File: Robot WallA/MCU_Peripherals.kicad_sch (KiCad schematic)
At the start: 44 parts, among them IC3 USBLC6-4SC6, IC4 USBLC6-4SC6, IC5 LAN8742A-CZ-TR, J2 USB4216-03-A, J3 SS-90000-009, T1 H1102NL

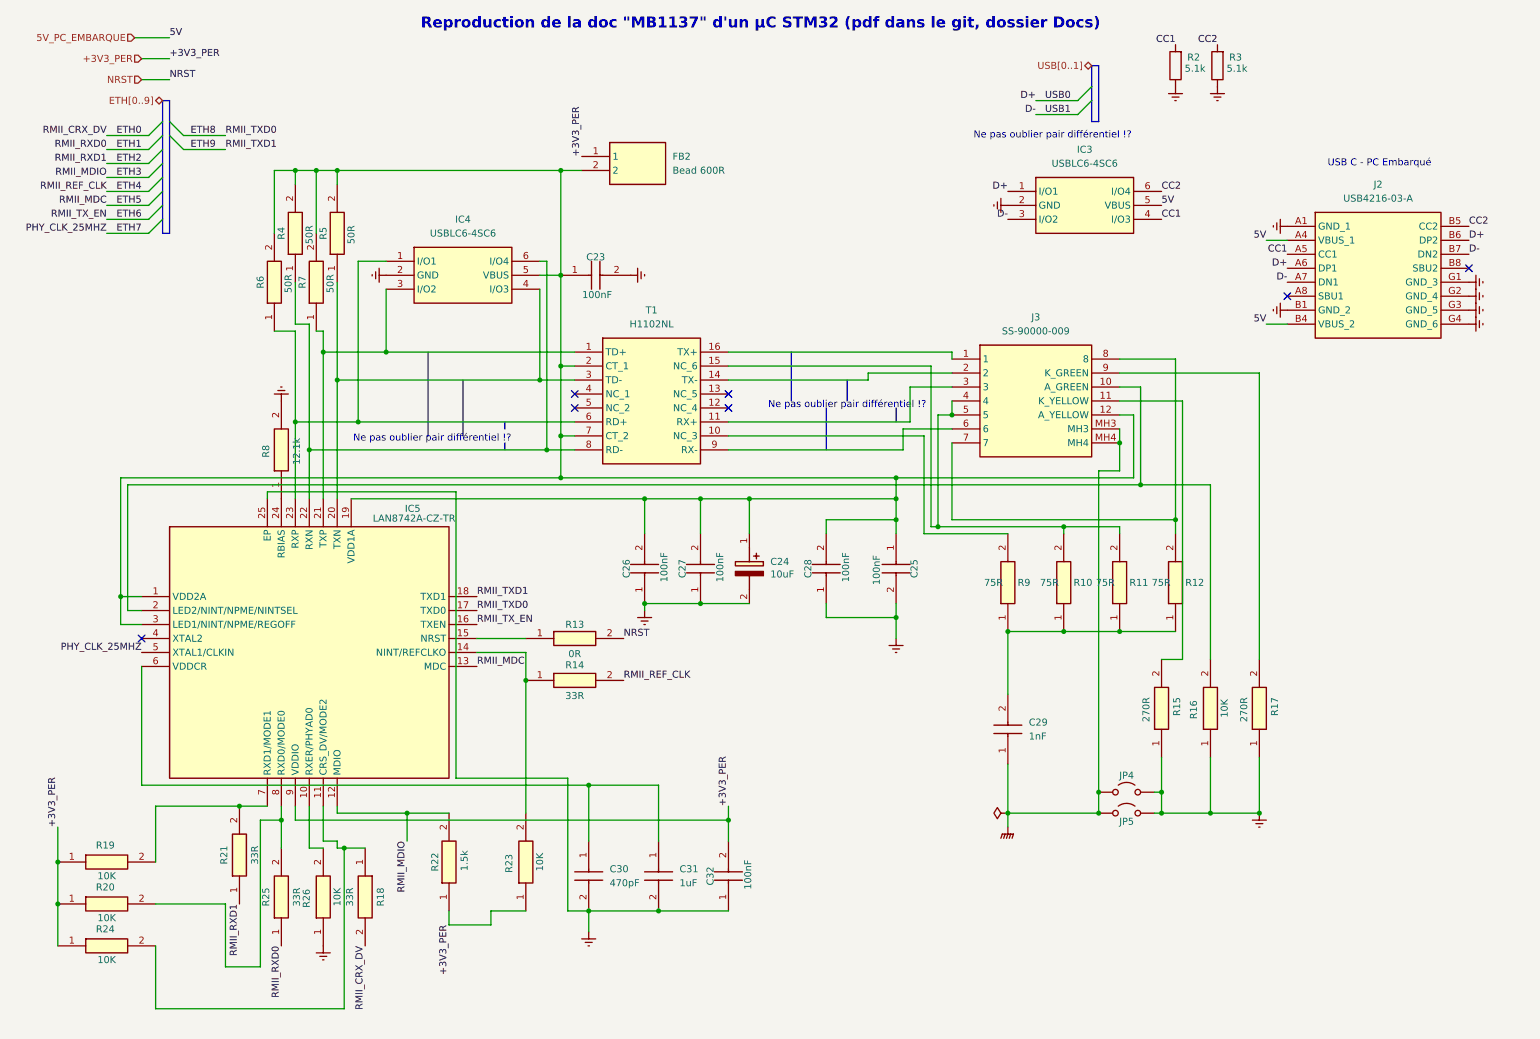
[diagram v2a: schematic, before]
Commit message: Begin to route ethenet, usb, 24V power supply.
Reworked Ethernet sheet because it was too hard to read
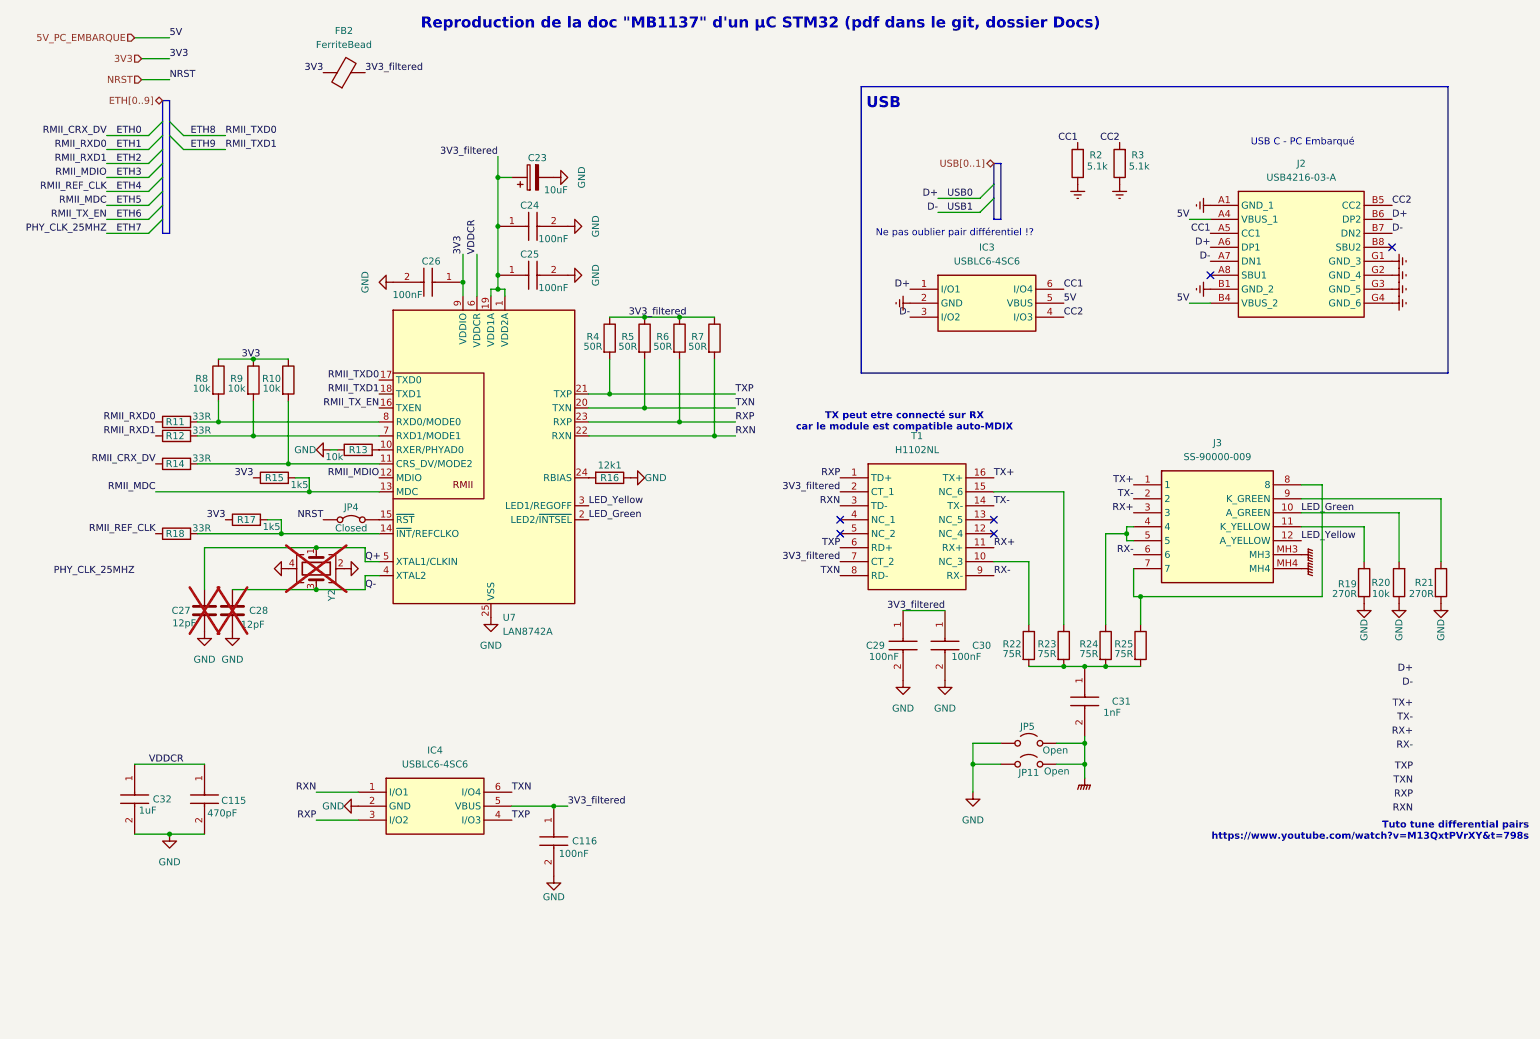
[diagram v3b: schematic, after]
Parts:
- removed C23, C25, C26, C27, C28, C32: 100nF, Capacitor_SMD:C_0603_1608Metric_Pad1.08x0.95mm_HandSolder, symbol SamacSys_Parts:CC0603KRX7R7BB104
- removed C24: 10uF, Capacitor_SMD:C_0603_1608Metric_Pad1.08x0.95mm_HandSolder, symbol SamacSys_Parts:TAJA106K016R
- removed C29: 1nF, Capacitor_SMD:C_0603_1608Metric_Pad1.08x0.95mm_HandSolder, symbol SamacSys_Parts:CC1206KKX7RDBB102
- removed C31: 1uF, Capacitor_SMD:C_0603_1608Metric_Pad1.08x0.95mm_HandSolder, symbol SamacSys_Parts:CC0603KRX5R7BB105
- removed FB2: Bead 600R, Resistor_SMD:R_0603_1608Metric_Pad0.98x0.95mm_HandSolder, symbol SamacSys_Parts:FCM1608KF-601T05
- removed IC5: LAN8742A-CZ-TR, SamacSys_Parts:QFN50P400X400X100-25N-D, symbol SamacSys_Parts:LAN8742A-CZ-TR
- removed JP4: SolderJumper, Jumper:SolderJumper-2_P1.3mm_Open_Pad1.0x1.5mm, symbol Jumper:Jumper_2_Open
- removed R10, R11, R12, R9: 75R, Resistor_SMD:R_0603_1608Metric_Pad0.98x0.95mm_HandSolder, symbol SamacSys_Parts:RC0603FR-0775RL
- removed R13: 0R, Resistor_SMD:R_0603_1608Metric_Pad0.98x0.95mm_HandSolder, symbol SamacSys_Parts:CRCW06030000Z0EI
- removed R14, R18, R21, R25: 33R, Resistor_SMD:R_0603_1608Metric_Pad0.98x0.95mm_HandSolder, symbol SamacSys_Parts:CRG0603F33R
- removed R15, R17: 270R, Resistor_SMD:R_0603_1608Metric_Pad0.98x0.95mm_HandSolder, symbol SamacSys_Parts:RC0603FR-07270RL
- removed R16, R19, R20, R23, R24, R26: 10K, Resistor_SMD:R_0603_1608Metric_Pad0.98x0.95mm_HandSolder, symbol SamacSys_Parts:CRCW060310K0FKEI
- removed R22: 1.5k, Resistor_SMD:R_0603_1608Metric_Pad0.98x0.95mm_HandSolder, symbol SamacSys_Parts:CRCW06031K50FKED
- removed R4, R5, R6, R7: 50R, Resistor_SMD:R_0603_1608Metric_Pad0.98x0.95mm_HandSolder, symbol SamacSys_Parts:TNPW060350R0DEEA
- removed R8: 12.1k, Resistor_SMD:R_0603_1608Metric_Pad0.98x0.95mm_HandSolder, symbol SamacSys_Parts:ERJ-P03F1212V
- added C115: 470pF, Capacitor_SMD:C_0603_1608Metric_Pad1.08x0.95mm_HandSolder, symbol SamacSys_Parts:CC0603JRNPO9BN471
- added C116, C24, C25, C26, C29: 100nF, Capacitor_SMD:C_0603_1608Metric_Pad1.08x0.95mm_HandSolder, symbol SamacSys_Parts:CC0603JRNPO9BN471
- added C23: 10uF, Capacitor_SMD:C_1206_3216Metric_Pad1.33x1.80mm_HandSolder, symbol Device:C_Polarized
- added C27, C28: 12pF, Capacitor_SMD:C_0603_1608Metric_Pad1.08x0.95mm_HandSolder, symbol Device:C
- added C31: 1nF, Capacitor_SMD:C_1206_3216Metric_Pad1.33x1.80mm_HandSolder, symbol SamacSys_Parts:CC0603JRNPO9BN471
- added C32: 1uF, Capacitor_SMD:C_0603_1608Metric_Pad1.08x0.95mm_HandSolder, symbol SamacSys_Parts:CC0603JRNPO9BN471
- added FB2: FerriteBead, Resistor_SMD:R_0603_1608Metric_Pad0.98x0.95mm_HandSolder, symbol Device:FerriteBead
- added JP11: Open, Jumper:SolderJumper-2_P1.3mm_Open_RoundedPad1.0x1.5mm, symbol Jumper:Jumper_2_Open
- added JP4: Closed, Jumper:SolderJumper-2_P1.3mm_Bridged_RoundedPad1.0x1.5mm, symbol Jumper:Jumper_2_Bridged
- added R10, R13, R20, R8, R9: 10k, Resistor_SMD:R_0603_1608Metric, symbol Device:R
- added R11, R12, R14, R18: 33R, Resistor_SMD:R_0603_1608Metric, symbol Device:R
- added R15, R17: 1k5, Resistor_SMD:R_0603_1608Metric, symbol Device:R
- added R16: 12k1, Resistor_SMD:R_0603_1608Metric, symbol Device:R
- added R19, R21: 270R, Resistor_SMD:R_0603_1608Metric, symbol Device:R
- added R22, R23, R24, R25: 75R, Resistor_SMD:R_0603_1608Metric, symbol Device:R
- added R4, R5, R6, R7: 50R, Resistor_SMD:R_0603_1608Metric, symbol Device:R
- added U7: LAN8742A, Package_DFN_QFN:VQFN-24-1EP_4x4mm_P0.5mm_EP2.5x2.5mm_ThermalVias, symbol Interface_Ethernet:LAN8742A
- added Y2: Crystal_GND24, Crystal:Crystal_SMD_3225-4Pin_3.2x2.5mm, symbol Device:Crystal_GND24
- C30: value 470pF -> 100nF
- JP5: value SolderJumper -> Open; footprint Jumper:SolderJumper-2_P1.3mm_Open_Pad1.0x1.5mm -> Jumper:SolderJumper-2_P1.3mm_Open_RoundedPad1.0x1.5mm
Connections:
- net CC1: now also IC3.6 (I/O4); no longer IC3.4 (I/O3)
- net CC2: now also IC3.4 (I/O3); no longer IC3.6 (I/O4)
- net ETH0: now also R14.1
- net ETH1: now also R11.1
- net ETH2: now also R12.1
- net ETH3: now also U7.12 (MDIO)
- net ETH4: now also R18.1
- net ETH5: now also R15.2, U7.13 (MDC)
- net ETH6: now also U7.16 (TXEN)
- net ETH8: now also U7.17 (TXD0)
- net ETH9: now also U7.18 (TXD1)
- net GNDPWR: now also C31.2, JP11.1 (A)
- net GNDREF: no longer C30.2, IC4.2 (GND), JP5.2 (B)
- net NRST: now also JP4.1 (A)
- net 3V3_filtered: now reaches IC4.5 (VBUS), T1.2 (CT_1), T1.7 (CT_2)
- net 3V3_filtered: now also C30.1, C116.1, C23.1, C24.1, C25.1, C29.1, FB2.2, R4.1, R5.1, R6.1, R7.1, U7.1 (VDD2A), U7.19 (VDD1A); no longer J3.12 (A_YELLOW)
- net TXN: now reaches IC4.6 (I/O4), T1.8 (RD-)
- net TXN: now also R5.2, U7.20 (TXN)
- net RXP: now reaches IC4.3 (I/O2), T1.1 (TD+)
- net RXP: now also R6.2, U7.23 (RXP)
- net at T1.10 (NC_3): now also R22.1
- net RX+: now reaches J3.3, T1.11 (RX+)
- net TX-: now reaches J3.2, T1.14 (TX-)
- net at J3.4, J3.5: now also R24.1; no longer T1.15 (NC_6)
- net TX+: now reaches J3.1, T1.16 (TX+)
- net RXN: now reaches T1.3 (TD-)
- net RXN: now also IC4.1 (I/O1), R7.2, U7.22 (RXN); no longer IC4.4 (I/O3)
- net TXP: now reaches T1.6 (RD+)
- net TXP: now also IC4.4 (I/O3), R4.2, U7.21 (TXP); no longer IC4.1 (I/O1)
- net RX-: now reaches J3.6, T1.9 (RX-)
- net LED_Green: now reaches J3.10 (A_GREEN)
- net LED_Green: now also R20.2, U7.2 (LED2/~{INTSEL})
- net at J3.7, J3.8: now also R25.1
- net at J3.11 (K_YELLOW): now also R19.1
- net at J3.9 (K_GREEN): now also R21.1
- new net: R13.2, U7.10 (RXER/PHYAD0)
- new net: R10.2, R14.2, U7.11 (CRS_DV/MODE2)
- new net: R17.2, R18.2, U7.14 (~{INT}/REFCLKO)
- new net: JP4.2 (B), U7.15 (~{RST})
- new net: R16.2, U7.24 (RBIAS)
- new net: R12.2, R9.2, U7.7 (RXD1/MODE1)
- new net: R11.2, R8.2, U7.8 (RXD0/MODE0)
- new net: C31.1, R22.2, R23.2, R24.2, R25.2
- new net: R23.1, T1.15 (NC_6)
- new net 3V3: C26.1, FB2.1, R10.1, R15.1, R17.1, R8.1, R9.1, U7.9 (VDDIO)
- new net GND: C115.2, C116.2, C23.2, C24.2, C25.2, C26.2, C27.2, C28.2, C29.2, C30.2, C32.2, IC4.2 (GND), JP11.2 (B), JP5.2 (B), R13.1, R16.1, R19.2, R20.1, R21.2, U7.25 (VSS), Y2.2, Y2.4
- new net LED_Yellow: J3.12 (A_YELLOW), U7.3 (LED1/REGOFF)
- new net Q+: C27.1, U7.5 (XTAL1/CLKIN), Y2.1
- new net Q-: C28.1, U7.4 (XTAL2), Y2.3
- new net VDDCR: C115.1, C32.1, U7.6 (VDDCR)
- no-connect marks 7 -> 6
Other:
- note added: "TX peut etre connecté sur RX car le module est compatible auto-MDIX"
- note added: "Tuto tune differential pairs https://www.youtube.com/watch?v=M13QxtPVrXY&t=798s"
- note added: "USB"
- moved on the sheet: IC3, J2, R2, R3

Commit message: Conitnue routing
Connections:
- net Q+ is gone; now on net ETH7: C27.1, U7.5 (XTAL1/CLKIN), Y2.1
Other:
- note removed: "Ne pas oublier pair différentiel !?"
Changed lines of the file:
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@@
-		)
-	)
-	(text "Ne pas oublier pair différentiel !?"
-		(exclude_from_sim no)
-		(at 179.578 54.61 0)
-		(effects
-			(font
-				(size 1.27 1.27)
-			)
 		)
 	)
@@
 	)
 	(label "PHY_CLK_25MHZ"
-		(at 30.48 116.84 180)
+		(at 43.18 115.57 180)
 		(effects
 			(font

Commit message: Correct a lot of error in DRC
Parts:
- U7: footprint Package_DFN_QFN:VQFN-24-1EP_4x4mm_P0.5mm_EP2.5x2.5mm_ThermalVias -> SamacSys_Parts:QFN50P400X400X100-25N-D
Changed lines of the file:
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@@
 			)
 		)
-		(property "Footprint" "Package_DFN_QFN:VQFN-24-1EP_4x4mm_P0.5mm_EP2.5x2.5mm_ThermalVias"
+		(property "Footprint" "SamacSys_Parts:QFN50P400X400X100-25N-D"
 			(at 96.52 123.19 0)
 			(effects

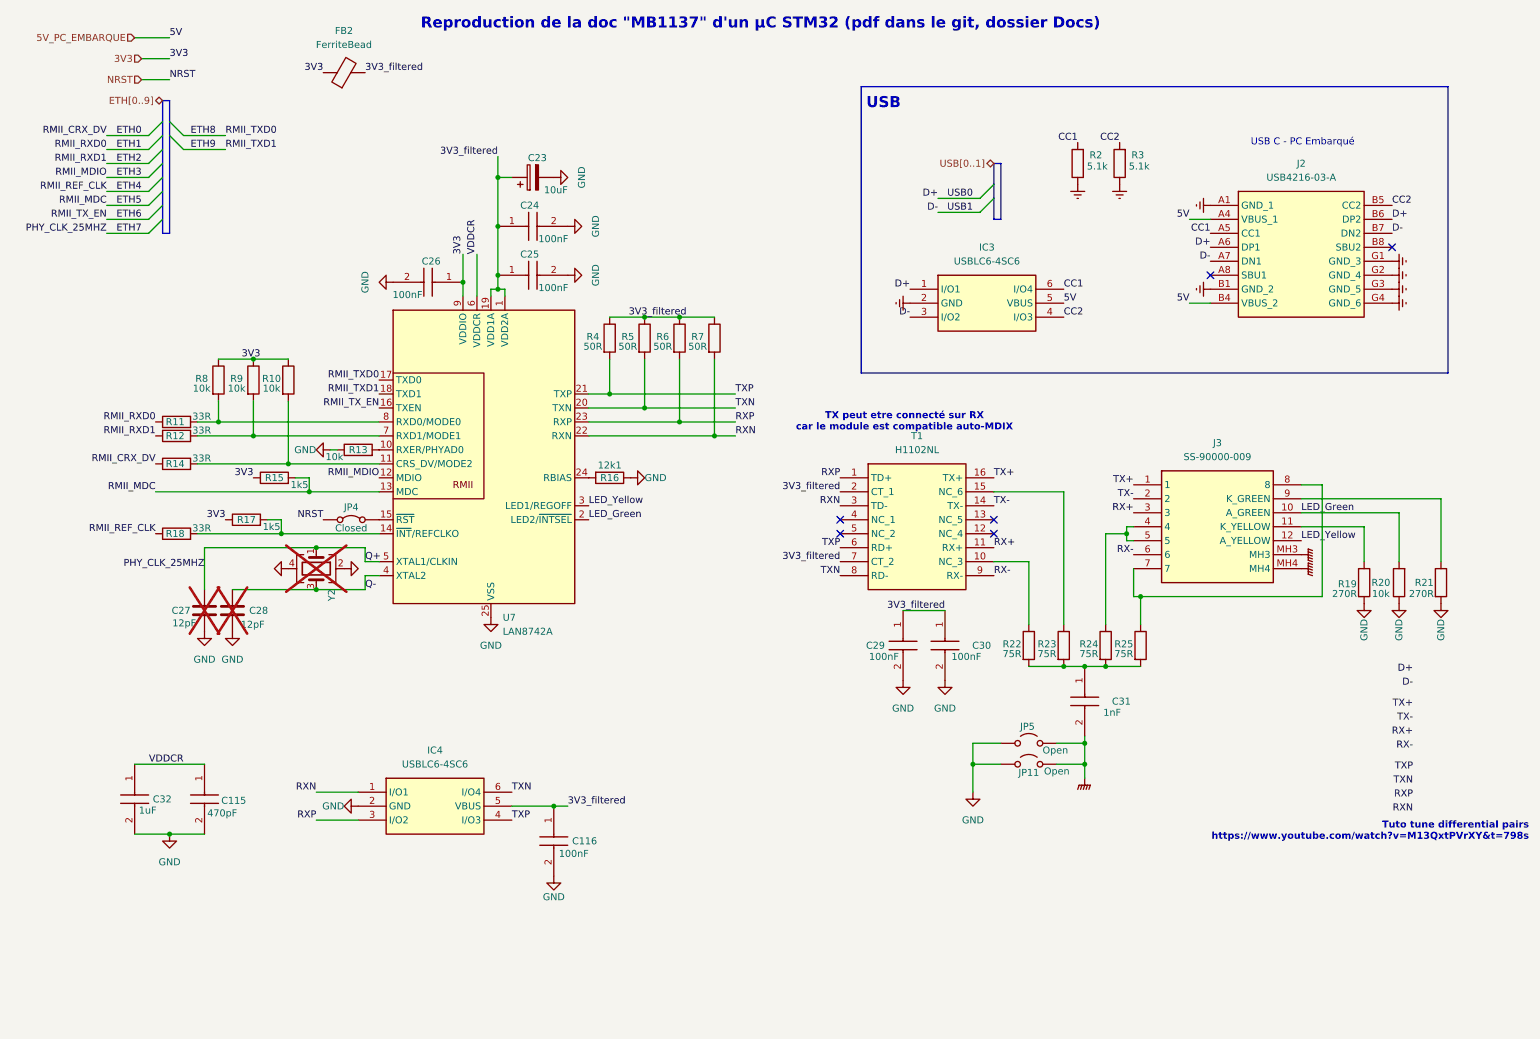
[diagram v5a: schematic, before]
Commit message: Corrected all DRC erros, added info on PCB
modified distance meter connectors to be horizontal
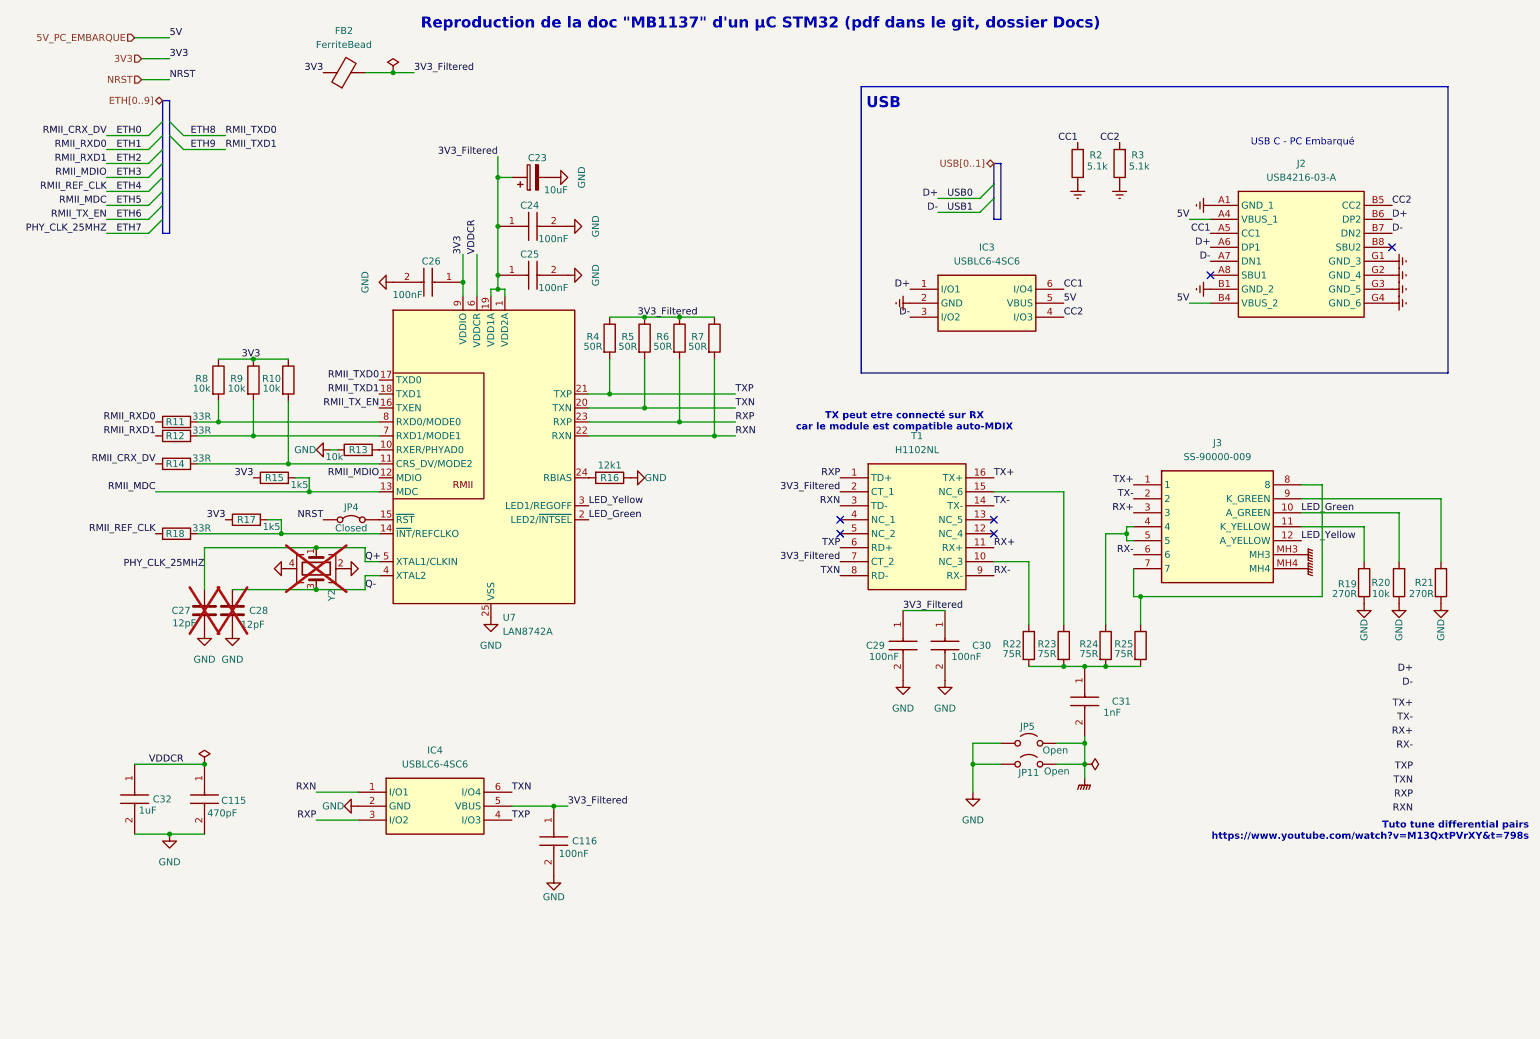
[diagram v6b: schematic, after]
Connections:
- net 3V3_filtered renamed 3V3_Filtered

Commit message: Updated fab files.
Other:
- company: (none) -> Socotec Monitoring
- title: (none) -> Robot Wall-A
